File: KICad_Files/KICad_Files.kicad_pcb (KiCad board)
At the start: 2 copper layers, 30 x 34 mm, 42 parts, among them J1 Conn_01x03_MountingPin, J2 Conn_01x03_MountingPin, J3 Conn_01x03_MountingPin, J4 USB_C_Receptacle_USB2.0_14P, J5 Conn_01x06, J6 Conn_01x06, J7 Conn_01x03_Pin, J8 Conn_01x03_Pin, SW1 RESET, SW2 RESET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

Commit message: added board settings to the project file
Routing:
- net GND: track 14.5 -> 13.9 mm
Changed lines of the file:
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@@
 		(tags "capacitor handsolder")
 		(property "Reference" "C7"
-			(at 0.75 1.5 360)
+			(at 0.75 1.5 0)
 			(layer "F.SilkS")
 			(effects
@@
 		)
 		(property "Value" "3p3"
-			(at 0 1.43 360)
+			(at 0 1.43 0)
 			(layer "F.Fab")
 			(effects
@@
 		)
 		(fp_text user "${REFERENCE}"
-			(at 0 0 360)
+			(at 0 0 0)
 			(layer "F.Fab")
 			(effects
@@
 		)
 		(fp_text user "${REFERENCE}"
-			(at 0 2 360)
+			(at 0 2 0)
 			(layer "F.Fab")
 			(effects
@@
 		)
 		(fp_text user "${REFERENCE}"
-			(at 0 2 360)
+			(at 0 2 0)
 			(layer "F.Fab")
 			(effects
@@
 		(tags "SOT TO_SOT_SMD")
 		(property "Reference" "U1"
-			(at -2.7625 -0.05 360)
+			(at -2.7625 -0.05 0)
 			(layer "F.SilkS")
 			(effects
@@
 		)
 		(property "Value" "Antenna_Chip"
-			(at 0 2.05 360)
+			(at 0 2.05 0)
 			(layer "F.Fab")
 			(effects
@@
 		)
 		(fp_text user "${REFERENCE}"
-			(at 0 0 360)
+			(at 0 0 0)
 			(layer "F.Fab")
 			(effects
@@
 		)
 		(property "Value" "100"
-			(at 0 1.43 360)
+			(at 0 1.43 0)
 			(layer "F.Fab")
 			(effects
@@
 		)
 		(fp_text user "${REFERENCE}"
-			(at 0 0 360)
+			(at 0 0 0)
 			(layer "F.Fab")
 			(effects
@@
 		(tags "resistor handsolder")
 		(property "Reference" "R9"
-			(at 0 1.25 360)
+			(at 0 1.25 0)
 			(layer "F.SilkS")
 			(effects
@@
 		)
 		(property "Value" "100"
-			(at 0 1.43 360)
+			(at 0 1.43 0)
 			(layer "F.Fab")
 			(effects
@@
 		)
 		(fp_text user "${REFERENCE}"
-			(at 0 0 360)
+			(at 0 0 0)
 			(layer "F.Fab")
 			(effects
@@
 		)
 		(property "Value" "3p3"
-			(at 0 1.43 360)
+			(at 0 1.43 0)
 			(layer "F.Fab")
 			(effects
@@
 		)
 		(fp_text user "${REFERENCE}"
-			(at 0 0 360)
+			(at 0 0 0)
 			(layer "F.Fab")
 			(effects
@@
 		(tags "capacitor handsolder")
 		(property "Reference" "C5"
-			(at 2.7 -0.05 360)
+			(at 2.7 -0.05 0)
 			(layer "B.SilkS")
 			(effects
@@
 		)
 		(property "Value" "22  μF"
-			(at 0 -1.43 360)
+			(at 0 -1.43 0)
 			(layer "B.Fab")
 			(effects
@@
 		)
 		(fp_text user "${REFERENCE}"
-			(at 0 0 360)
+			(at 0 0 0)
 			(layer "B.Fab")
 			(effects
@@
 		(tags "capacitor handsolder")
 		(property "Reference" "C2"
-			(at -0.05 1.2 360)
+			(at -0.05 1.2 0)
 			(layer "B.SilkS")
 			(effects
@@
 		)
 		(property "Value" "10 uF"
-			(at 0 -1.43 360)
+			(at 0 -1.43 0)
 			(layer "B.Fab")
 			(effects
@@
 		)
 		(fp_text user "${REFERENCE}"
-			(at 0 0 360)
+			(at 0 0 0)
 			(layer "B.Fab")
 			(effects
@@
 		)
 		(property "Value" "100 nF"
-			(at 0 -1.43 360)
+			(at 0 -1.43 0)
 			(layer "B.Fab")
 			(effects
@@
 		)
 		(fp_text user "${REFERENCE}"
-			(at 0 0 360)
+			(at 0 0 0)
 			(layer "B.Fab")
 			(effects
@@
 		(tags "capacitor handsolder")
 		(property "Reference" "C4"
-			(at 2.6 -0.1 360)
+			(at 2.6 -0.1 0)
 			(layer "B.SilkS")
 			(effects
@@
 		)
 		(property "Value" "22 μF"
-			(at 0 -1.43 360)
+			(at 0 -1.43 0)
 			(layer "B.Fab")
 			(effects
@@
 		)
 		(fp_text user "${REFERENCE}"
-			(at 0 0 360)
+			(at 0 0 0)
 			(layer "B.Fab")
 			(effects
@@
 	)
 	(segment
-		(start 130 40.4)
-		(end 130.2 40.4)
-		(width 0.2)
-		(layer "F.Cu")
-		(net 4)
-	)
-	(segment
-		(start 130.2 40.4)
-		(end 130.5 40.7)
-		(width 0.2)
-		(layer "F.Cu")
-		(net 4)
-	)
-	(segment
 		(start 138.6 43.4)
 		(end 138.6 44)
@@
 	)
 	(via
-		(at 130.5 40.7)
+		(at 130 40.4)
 		(size 0.6)
 		(drill 0.3)

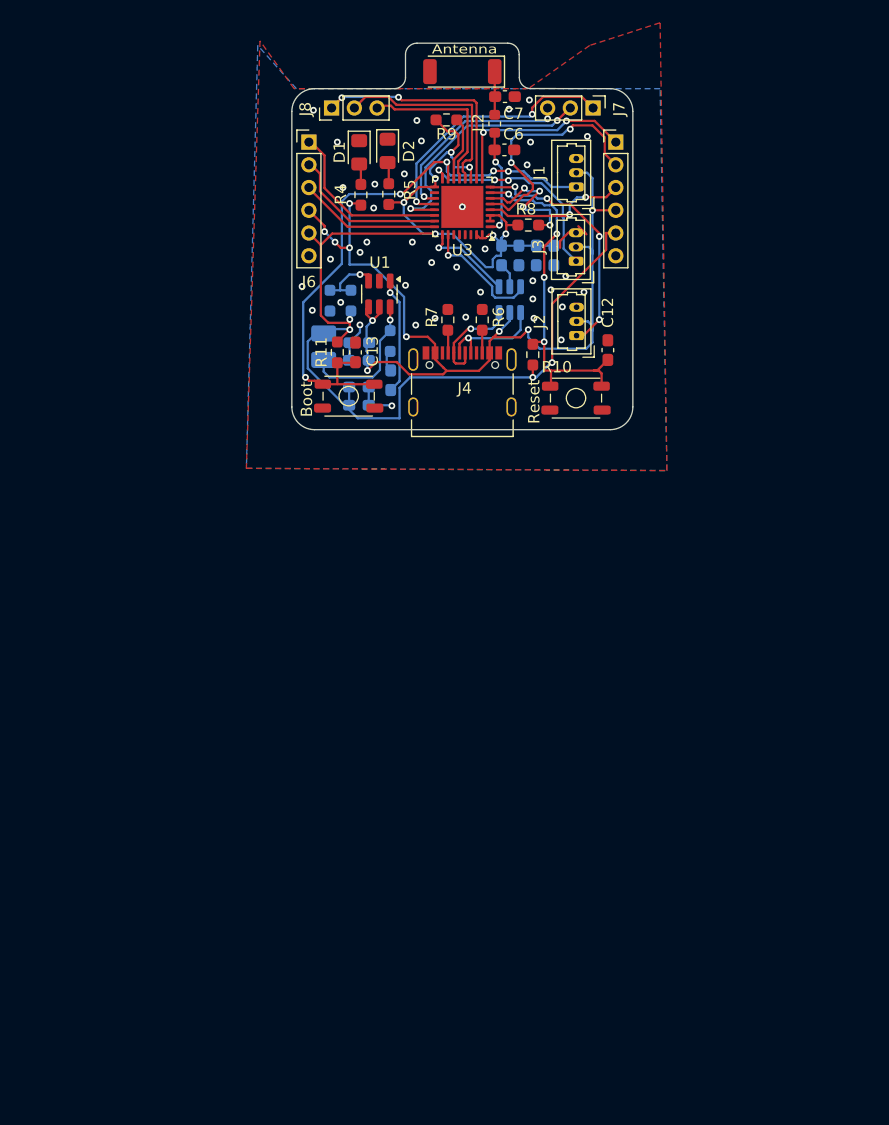
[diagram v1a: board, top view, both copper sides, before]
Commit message: adjusted vias for better ground plane flow
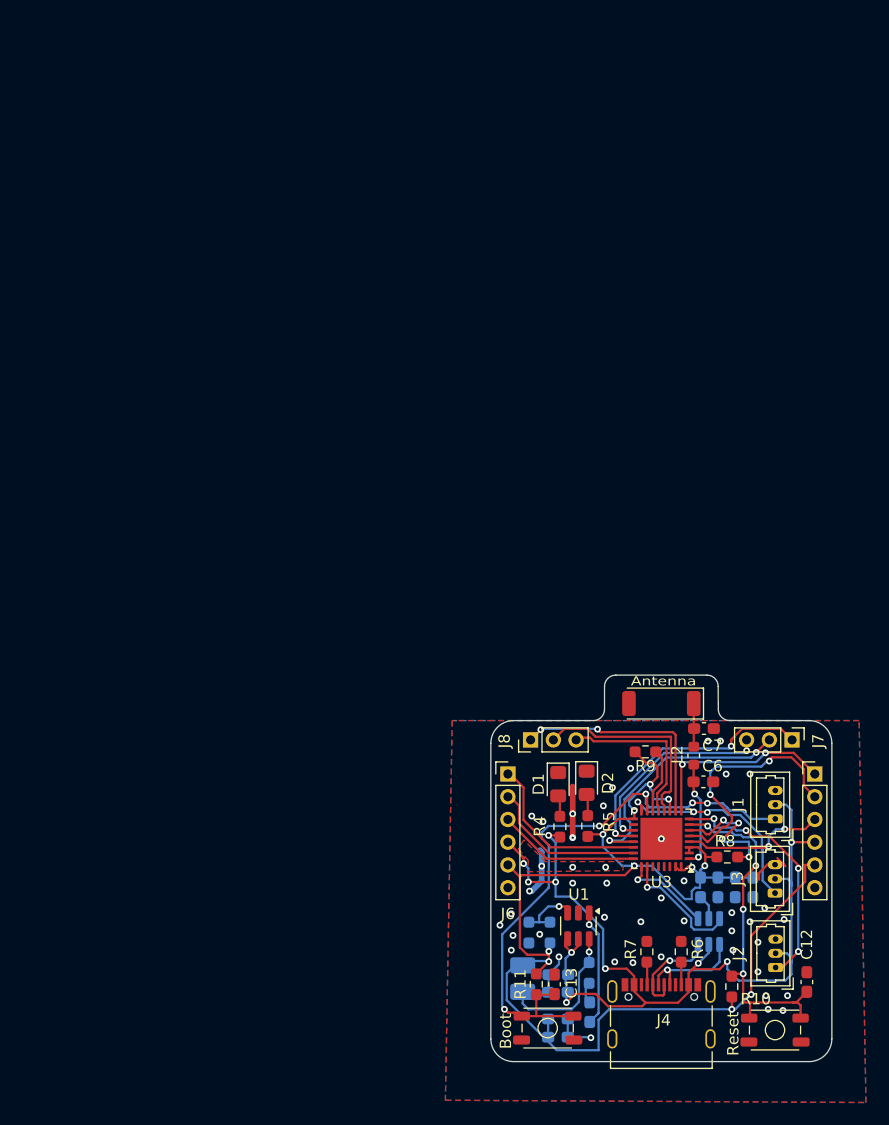
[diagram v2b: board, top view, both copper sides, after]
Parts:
- moved AE1 58.3 mm to (147.5, 84.1)
- moved C10 58.3 mm to (152.5, 100.3)
- moved C11 58.3 mm to (155.6, 100.3)
- moved C12 58.3 mm to (160.3, 108.6)
- moved C4 58.3 mm to (138.4, 111.8)
- moved C8 58.3 mm to (151.0, 100.3)
- moved C9 58.3 mm to (154.0, 100.3)
- moved J3 58.3 mm to (157.5, 100.8)
- moved R8 58.3 mm to (153.3, 97.6)
- moved R9 58.3 mm to (146.1, 88.3)
- moved SW2 58.3 mm to (137.5, 112.6)
- moved U1 58.3 mm to (140.2, 103.7)
- moved U2 58.3 mm to (151.7, 104.2)
- moved C1 58.3 mm to (141.2, 111.2)
- moved C2 58.3 mm to (138.4, 109.5)
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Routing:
- net GND: track 13.9 -> 22.6 mm, vias 39 -> 45
- net +5V: track 84.0 -> 85.0 mm
- net /LED3: track 52.2 -> 52.7 mm

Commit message: rework of the PCB Layout
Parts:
- C1, C10, C11, C2, C3, C4, C5, C8, C9, L1, R1, R2, R3, U2: moved to F.Cu
- R6, R7: moved to B.Cu
- R8, R9: value 100 -> 10kΩ
- SW1: value RESET -> Reset
- SW2: value RESET -> Boot
- moved J5 67.7 mm to (93.3, 88.9)
- moved J2 61.4 mm to (98.0, 92.8)
- moved J1 59.8 mm to (98.0, 99.3)
- moved J3 59.8 mm to (98.0, 105.8)
- moved C9 52.6 mm to (102.3, 90.7), turned to 180 degrees
- moved R8 51.5 mm to (102.1, 92.4)
- moved C11 47.2 mm to (109.2, 91.7), turned to -45 degrees
- moved C7 46.7 mm to (104.5, 85.7), turned to 180 degrees
- moved R9 44.9 mm to (102.0, 97.0), turned to -45 degrees
- moved U2 44.9 mm to (106.8, 103.2)
- moved L2 44.9 mm to (105.5, 88.0)
- moved C12 44.0 mm to (116.3, 108.3), turned to 0 degrees
- moved C6 43.4 mm to (107.9, 88.8)
- moved C13 42.7 mm to (95.4, 108.6), turned to 0 degrees
- moved C10 42.5 mm to (111.6, 88.8), turned to 45 degrees
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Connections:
- J7 pad 1: /GPIO 13 -> /GPIO 14
- J7 pad 2: /GPIO 14 -> /GPIO 13
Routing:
- net /LED3: track 52.7 -> 27.0 mm, vias 5 -> 1
- net /LED2: track 22.4 -> 6.46 mm, vias 4 -> 1
- net Net-(U3-GPIO2): track 12.0 -> 1.99 mm, vias 4 -> 0
- net Net-(U3-CHIP_EN): track 31.9 -> 40.3 mm
- net Net-(U1-VBST): track 10.3 -> 1.92 mm, vias 1 -> 0
- net GND: track 22.6 -> 30.6 mm, vias 45 -> 67
- net +5V: track 85.0 -> 77.5 mm, vias 10 -> 6
- net D-: track 8.04 -> 14.6 mm, vias 1 -> 2
- net /GPIO 7: track 14.6 -> 21.1 mm, vias 0 -> 2
- net /GPIO 1: track 21.9 -> 15.5 mm, vias 2 -> 1
- net /GPIO 13: track 23.7 -> 17.4 mm, vias 2 -> 1
- net /Antenna: track 9.38 -> 4.16 mm, vias 2 -> 0
- net D+: track 10.8 -> 15.3 mm, vias 1 -> 2
- net /LED1: track 18.8 -> 15.0 mm, vias 3 -> 1
- net /GPIO 14: track 22.3 -> 18.5 mm, vias 2 -> 1
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
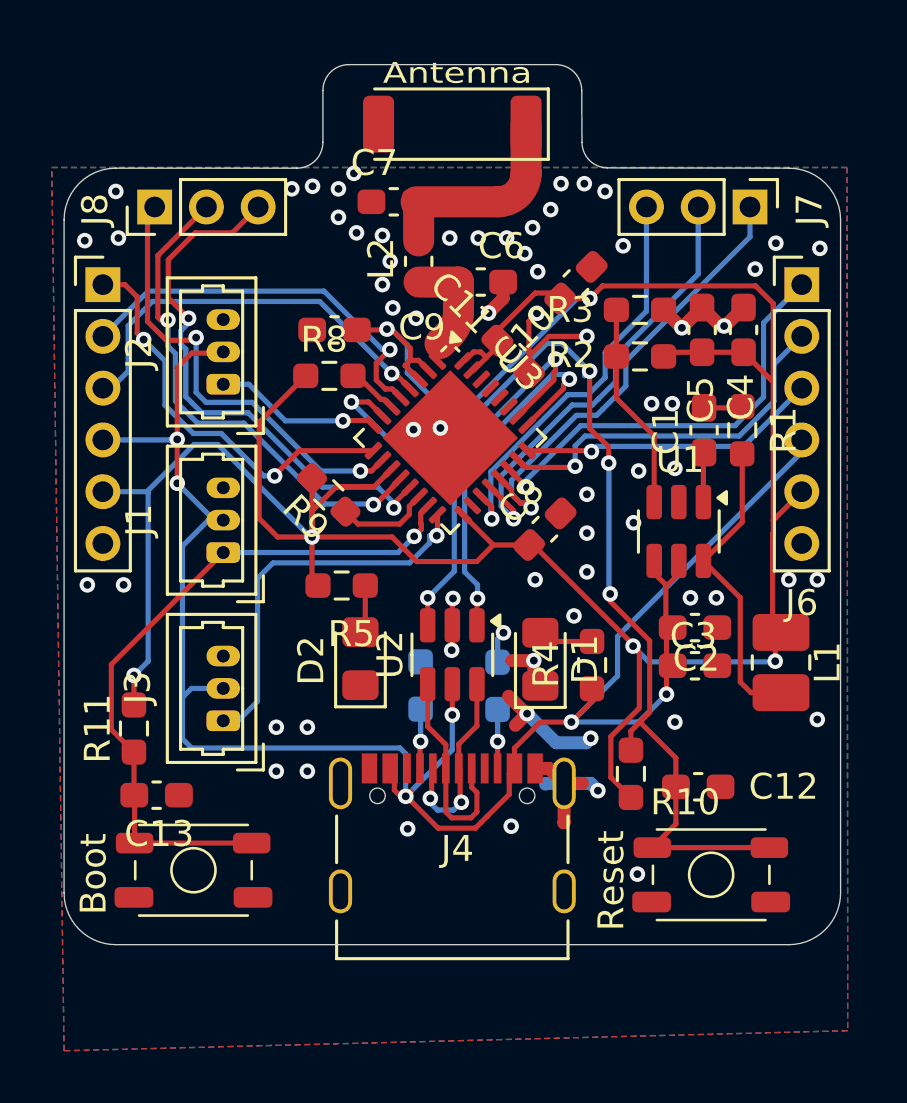
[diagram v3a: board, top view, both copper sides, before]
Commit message: fixed placement of silkscreen and improoved flow of the GND-plane
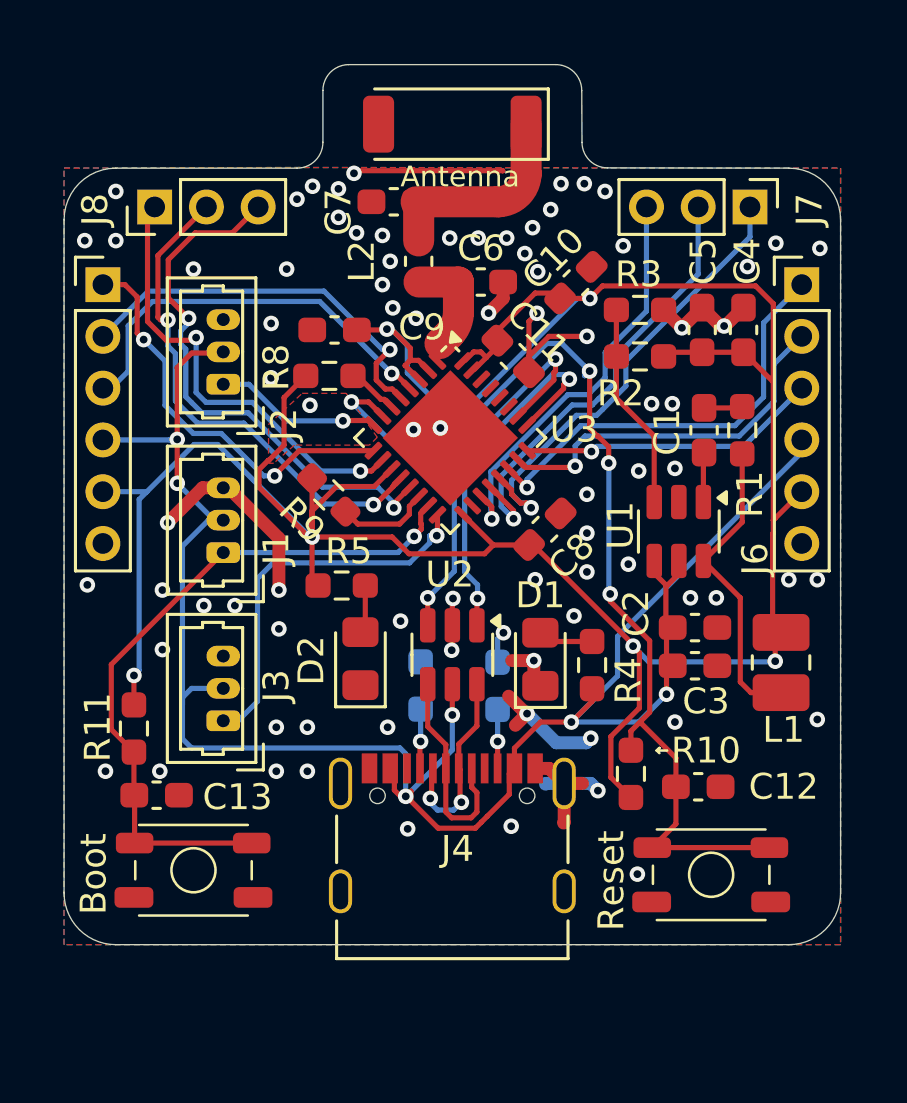
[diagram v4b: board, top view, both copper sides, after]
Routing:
- net GND: track 30.6 -> 44.1 mm, vias 67 -> 82
- net +3.3V: track 117.2 -> 116.2 mm

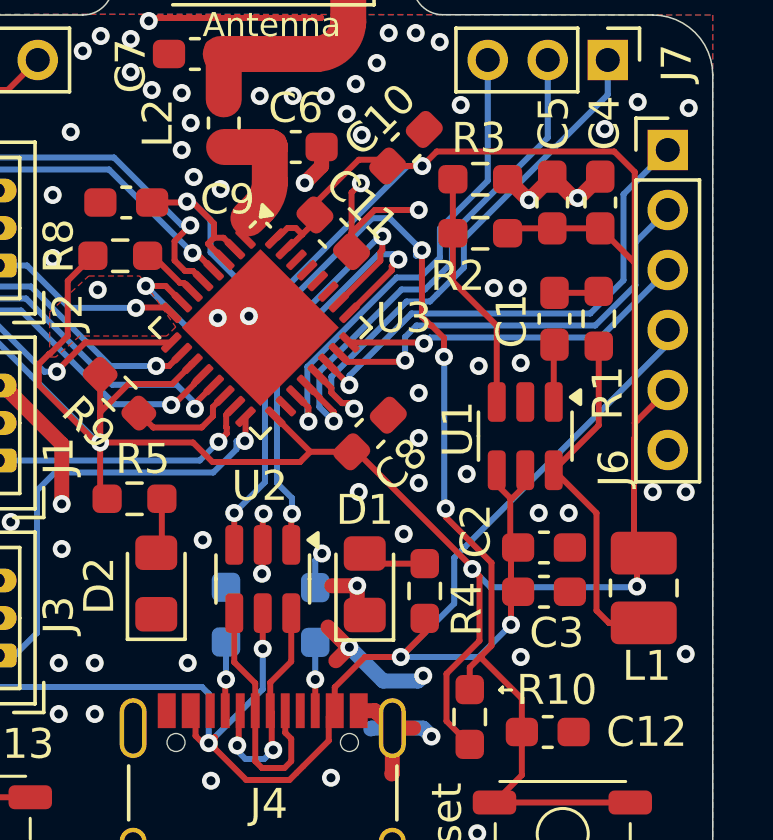
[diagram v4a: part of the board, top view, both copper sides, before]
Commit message: Added silkscreen Logo and Credits
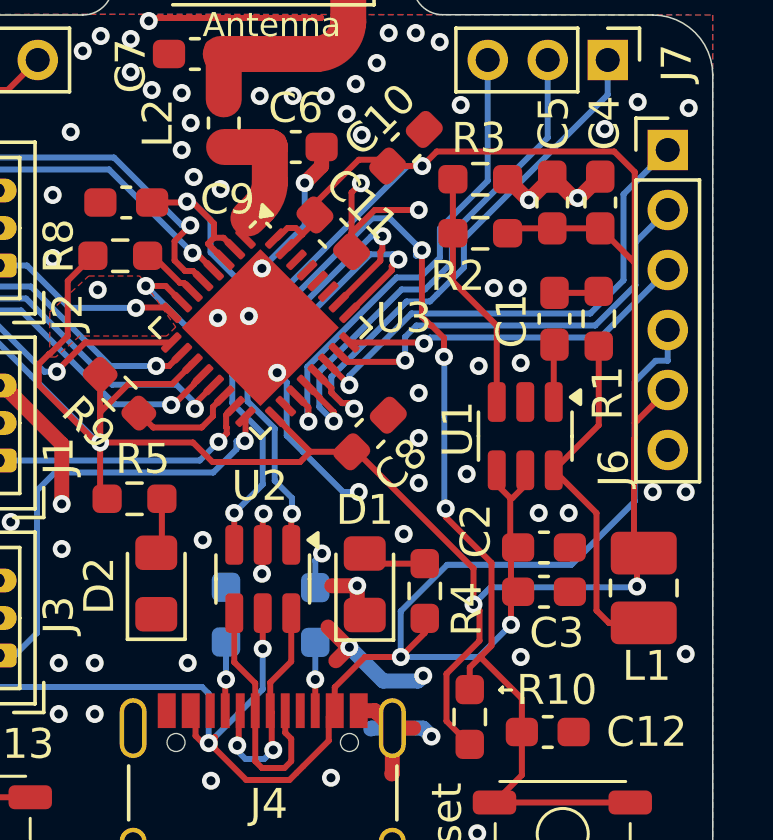
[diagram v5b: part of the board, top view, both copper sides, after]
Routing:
- net GND: track 44.1 -> 52.9 mm, vias 82 -> 84
- net +5V: track 77.5 -> 80.2 mm
- net D+: track 15.3 -> 16.3 mm
- net D-: track 14.6 -> 15.6 mm
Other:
- board text added: "ESP32-C3 LED-Devboard Made by Kideya Date: 01.2025 | Rev.1"
- board text added: "Git: Kideya/ESP32-C3-LED-Connector"
- board text added: "Netz39 e.V"

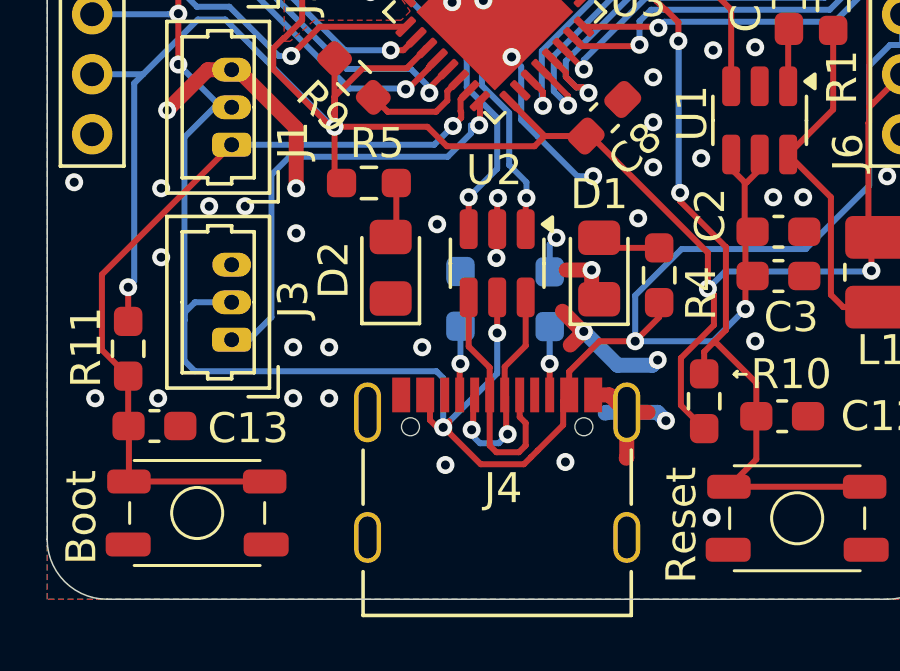
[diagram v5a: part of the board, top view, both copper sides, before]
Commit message: added names for the GPIO moved resistors for 5V USB to the front plane changed Logo from Nettz39 e.V. zu BlindDeerStudio Naming of GPIOS are still generic
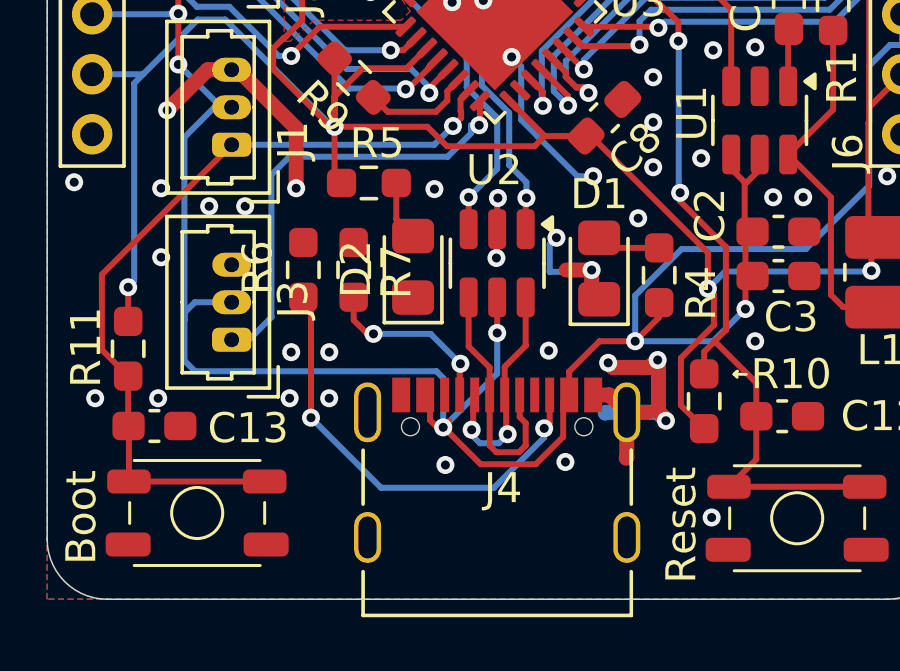
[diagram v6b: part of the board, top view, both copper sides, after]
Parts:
- R6, R7: moved to F.Cu
- moved R6 8.27 mm to (100.3, 103.4)
- moved R7 3.69 mm to (102.0, 103.4)
- moved D2 0.75 mm to (104.0, 103.3)
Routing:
- net Net-(J4-CC2): track 2.28 -> 15.0 mm, vias 1 -> 2
- net Net-(J4-CC1): track 2.30 -> 5.97 mm, vias 1 -> 2
- net GND: track 52.9 -> 52.2 mm, vias 84 -> 83
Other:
- board text added: "5V"
- board text added: "Blind-Deer Studio"
- board text added: "GND"
- board text added: "GPIO10/16"
- board text added: "GPIO4/9"
- board text added: "Github: Kideya/ESP32-C3-LED-Connector"
- board text removed: "Git: Kideya/ESP32-C3-LED-Connector"
- board text removed: "Netz39 e.V"
